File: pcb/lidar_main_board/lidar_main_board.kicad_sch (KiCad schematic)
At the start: 18 parts, among them J1 vl53l1x, J2 AS5600, J3 HC-06, J4 Bateria, U1 LPC845-BRK, U2 AMS1117-3.3, U3 LM7805_TO220

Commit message: add pcb
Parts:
- added A1: Pololu_Breakout_A4988, Module:Pololu_Breakout-16_15.2x20.3mm, symbol Driver_Motor:Pololu_Breakout_A4988
- added D2: LED, LED_THT:LED_D5.0mm, symbol Device:LED
- added J5: Boton 1, Connector_PinHeader_2.54mm:PinHeader_1x03_P2.54mm_Vertical, symbol Connector:Conn_01x03_Pin
- added J6: Boton 2, Connector_PinHeader_2.54mm:PinHeader_1x03_P2.54mm_Vertical, symbol Connector:Conn_01x03_Pin
- added J7: Boton 3, Connector_PinHeader_2.54mm:PinHeader_1x03_P2.54mm_Vertical, symbol Connector:Conn_01x03_Pin
- added J8: Motor, Connector_PinHeader_2.54mm:PinHeader_1x04_P2.54mm_Vertical, symbol Connector:Conn_01x04_Pin
- added R2: 33k, Resistor_THT:R_Axial_DIN0207_L6.3mm_D2.5mm_P10.16mm_Horizontal, symbol Device:R
- added R3: 20k, Resistor_THT:R_Axial_DIN0207_L6.3mm_D2.5mm_P10.16mm_Horizontal, symbol Device:R
- added R4: 120, Resistor_THT:R_Axial_DIN0207_L6.3mm_D2.5mm_P10.16mm_Horizontal, symbol Device:R
- D1: value LED -> LED_PWR
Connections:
- net +3V3: now also U1.40 (VDD), A1.13 (~{RESET}), A1.14 (~{SLEEP}), A1.2 (VDD), J5.1 (Pin_1), J6.1 (Pin_1), J7.1 (Pin_1), R4.1
- net +5V: now also J3.2 (Pin_2), A1.8 (VMOT); no longer J3.1 (Pin_1)
- net +BATT: now also J4.2 (Pin_2), R2.1; no longer J4.1 (Pin_1)
- net GND: now also J3.1 (Pin_1), J4.1 (Pin_1), U1.20 (GND), A1.1 (GND), A1.12 (MS3), A1.7 (GND), A1.9 (~{ENABLE}), J5.2 (Pin_2), J6.2 (Pin_2), J7.2 (Pin_2), R3.2; no longer J3.2 (Pin_2), J4.2 (Pin_2)
- net I2C1 - SCL: now also J2.3 (Pin_3), U1.7 (PIO0_22); no longer J2.4 (Pin_4)
- net I2C1 - SDA: now also J2.4 (Pin_4), U1.8 (PIO0_23); no longer J2.3 (Pin_3)
- net UART0 - RX: now also U1.2 (PIO0_17)
- net UART0 - TX: now also U1.1 (PIO0_16)
- net BTN_START: now reaches U1.15 (PIO0_29)
- net BTN_START: now also J5.3 (Pin_3)
- net BTN_SEL: now reaches U1.16 (PIO0_30)
- net BTN_SEL: now also J7.3 (Pin_3)
- net BTN_MODE: now reaches U1.17 (PIO0_31)
- net BTN_MODE: now also J6.3 (Pin_3)
- net DIR: now reaches U1.23 (PIO0_10)
- net DIR: now also A1.16 (DIR)
- net STEP: now reaches U1.24 (PIO0_11)
- net STEP: now also A1.15 (STEP)
- net MS2: now reaches U1.28 (PIO0_15)
- net MS2: now also A1.11 (MS2)
- net MS1: now reaches U1.29 (PIO1_2_RED_LED)
- net MS1: now also A1.10 (MS1)
- net BAT_ADC: now reaches U1.33 (PIO0_06)
- net BAT_ADC: now also R2.2, R3.1
- net LED_DIR: now reaches U1.36 (PIO0_03_SWCLK)
- net LED_DIR: now also D2.1 (K)
- new net: D2.2 (A), R4.2
- new net: A1.3 (1B), J8.1 (Pin_1)
- new net: A1.4 (1A), J8.2 (Pin_2)
- new net: A1.5 (2A), J8.3 (Pin_3)
- new net: A1.6 (2B), J8.4 (Pin_4)
- no-connect marks 0 -> 25
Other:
- note added: "Bateria"
- note added: "Leds"
- note added: "R1= R2 [( Vcc / Vadc) - 1] R2 = 20K Vcc = 2 * 4.2V = 8.4V Vadc = 3.2 V R1 = 32K5 = 33K"
- note added: "Vd = 1.2 V Id = (Vcc - Vd)/R1 Id = 17.5mA"
- moved on the sheet: C1, C2, C3, C4, C5, D1, H1, H2, H3, H4, J1, J2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

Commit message: new version pcb
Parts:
- removed J2: AS5600, Connector_PinHeader_2.54mm:PinHeader_1x04_P2.54mm_Vertical, symbol Connector:Conn_01x04_Pin
- added D3: LED, LED_THT:LED_D5.0mm, symbol Device:LED
- added J2: AS5600, Connector_PinHeader_2.54mm:PinHeader_1x05_P2.54mm_Vertical, symbol Connector:Conn_01x05_Pin
- added R5: 120, Resistor_THT:R_Axial_DIN0207_L6.3mm_D2.5mm_P10.16mm_Horizontal, symbol Device:R
- D1: value LED_PWR -> LED
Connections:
- net +3V3: no longer A1.13 (~{RESET}), A1.14 (~{SLEEP}), R4.1
- net +5V: now also J2.1 (Pin_1)
- net +BATT: now also J4.1 (Pin_1); no longer J4.2 (Pin_2)
- net BTN_MODE: now also U1.16 (PIO0_30); no longer U1.17 (PIO0_31)
- net BTN_SEL: now also U1.17 (PIO0_31); no longer U1.16 (PIO0_30)
- net DIR: now also R4.1, U1.22 (PIO0_09); no longer U1.23 (PIO0_10)
- net GND: now also D2.1 (K), J4.2 (Pin_2), D3.1 (K), J2.2 (Pin_2); no longer A1.12 (MS3), J4.1 (Pin_1)
- net I2C1 - SCL: now also U1.6 (PIO0_21), J2.3 (Pin_3); no longer U1.7 (PIO0_22)
- net I2C1 - SDA: now also U1.7 (PIO0_22), J2.4 (Pin_4); no longer U1.8 (PIO0_23)
- net STEP: now also U1.23 (PIO0_10), R5.1; no longer U1.24 (PIO0_11)
- net DIR_AS5600: now reaches U1.12 (PIO0_26)
- net DIR_AS5600: now also J2.5 (Pin_5)
- net MRESET: now reaches U1.26 (PIO0_13)
- net MRESET: now also A1.13 (~{RESET})
- net MS3: now reaches U1.27 (PIO0_14)
- net MS3: now also A1.12 (MS3)
- net LED_DIR: no longer names the net of U1.36 (PIO0_03_SWCLK)
- net LED_DIR: no longer D2.1 (K)
- new net: D3.2 (A), R5.2
- new net MSLEEP: A1.14 (~{SLEEP}), U1.24 (PIO0_11)
- no-connect marks 25 -> 22
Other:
- note added: "Vd = 1.2 V Vcc = 3.3 V Id = (Vcc - Vd)/R1 Id = 17.5mA"
- note removed: "Vd = 1.2 V Id = (Vcc - Vd)/R1 Id = 17.5mA"
- moved on the sheet: D1, D2, H1, H2, H3, H4, J1, J3, J4, J5, J6, J7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

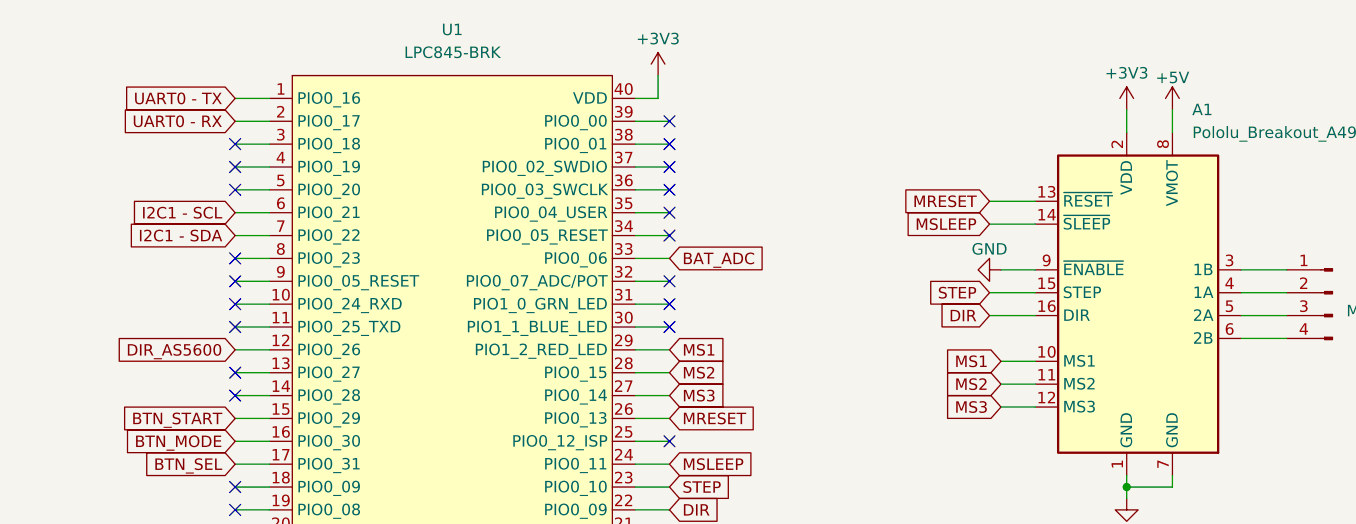
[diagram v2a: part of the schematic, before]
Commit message: molex in pcb
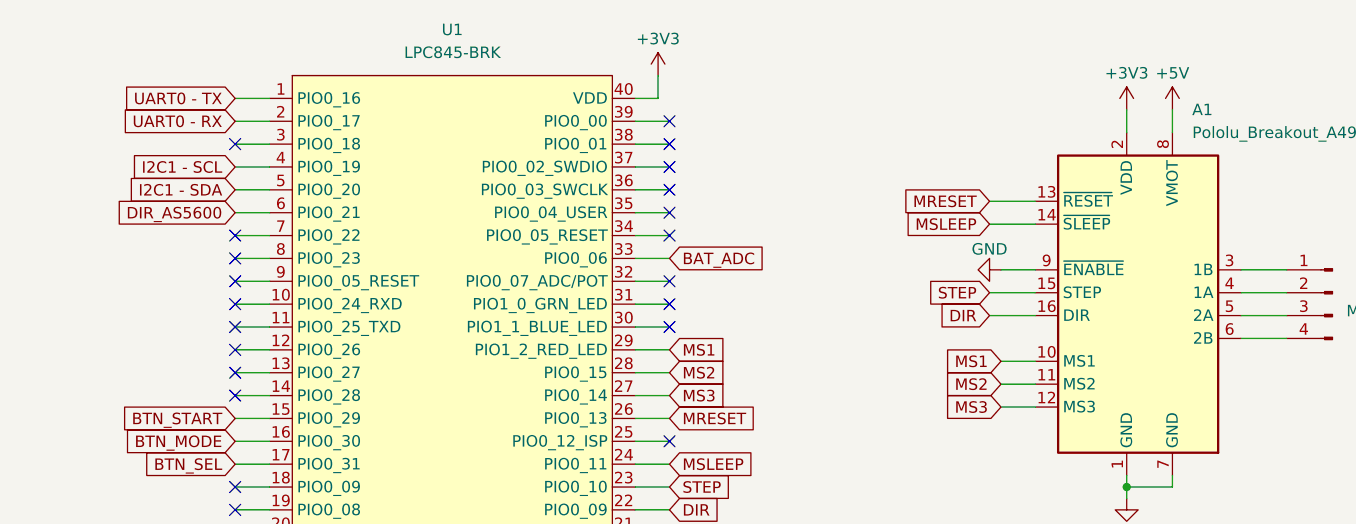
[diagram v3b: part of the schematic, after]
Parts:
- J1, J8: footprint Connector_PinHeader_2.54mm:PinHeader_1x04_P2.54mm_Vertical -> Connector_Molex:Molex_SL_171971-0004_1x04_P2.54mm_Vertical
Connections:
- net DIR_AS5600: now also U1.6 (PIO0_21); no longer U1.12 (PIO0_26)
- net I2C1 - SCL: now also U1.4 (PIO0_19); no longer U1.6 (PIO0_21)
- net I2C1 - SDA: now also U1.5 (PIO0_20); no longer U1.7 (PIO0_22)
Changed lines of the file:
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@@
 	)
 	(no_connect
-		(at 36.83 31.75)
+		(at 36.83 52.07)
 	)
 	(no_connect
-		(at 36.83 34.29)
+		(at 36.83 39.37)
 	)
 	(no_connect
@@
 	)
 	(no_connect
-		(at 36.83 29.21)
-	)
-	(no_connect
 		(at 85.09 31.75)
 	)
@@
 	)
 	(no_connect
+		(at 36.83 29.21)
+	)
+	(no_connect
 		(at 85.09 62.23)
 	)
@@
 		)
 	)
-	(global_label "MS1"
+	(global_label "DIR_AS5600"
 		(shape input)
-		(at 121.92 53.34 180)
+		(at 36.83 36.83 180)
 		(fields_autoplaced yes)
 		(effects
@@
 		)
 		(property "Intersheetrefs" "${INTERSHEET_REFS}"
-			(at 115.0644 53.34 0)
+			(at 22.5963 36.83 0)
 			(effects
 				(font
@@
 		)
 	)
-	(global_label "I2C1 - SCL"
+	(global_label "MS1"
 		(shape input)
-		(at 36.83 36.83 180)
+		(at 121.92 53.34 180)
 		(fields_autoplaced yes)
 		(effects
@@
 		)
 		(property "Intersheetrefs" "${INTERSHEET_REFS}"
-			(at 22.5358 36.83 0)
+			(at 115.0644 53.34 0)
 			(effects
 				(font
@@
 		)
 	)
-	(global_label "I2C1 - SCL"
+	(global_label "I2C1 - SDA"
 		(shape input)
-		(at 133.35 151.13 0)
+		(at 36.83 34.29 180)
 		(fields_autoplaced yes)
 		(effects
@@
 				(size 1.27 1.27)
 			)
-			(justify left)
+			(justify right)
 		)
 		(property "Intersheetrefs" "${INTERSHEET_REFS}"
-			(at 147.6442 151.13 0)
+			(at 22.4753 34.29 0)
 			(effects
 				(font
 					(size 1.27 1.27)
 				)
-				(justify left)
+				(justify right)
 				(hide yes)
 			)
 		)
 	)
-	(global_label "MSLEEP"
+	(global_label "I2C1 - SCL"
 		(shape input)
-		(at 120.65 38.1 180)
+		(at 133.35 151.13 0)
 		(fields_autoplaced yes)
 		(effects
@@
 				(size 1.27 1.27)
 			)
-			(justify right)
+			(justify left)
 		)
 		(property "Intersheetrefs" "${INTERSHEET_REFS}"
-			(at 110.4078 38.1 0)
+			(at 147.6442 151.13 0)
 			(effects
 				(font
 					(size 1.27 1.27)
 				)
-				(justify right)
+				(justify left)
 				(hide yes)
 			)
 		)
 	)
-	(global_label "DIR_AS5600"
+	(global_label "MSLEEP"
 		(shape input)
-		(at 36.83 52.07 180)
+		(at 120.65 38.1 180)
 		(fields_autoplaced yes)
 		(effects
@@
 		)
 		(property "Intersheetrefs" "${INTERSHEET_REFS}"
-			(at 22.5963 52.07 0)
+			(at 110.4078 38.1 0)
 			(effects
 				(font
@@
 		)
 	)
+	(global_label "I2C1 - SCL"
+		(shape input)
+		(at 36.83 31.75 180)
+		(fields_autoplaced yes)
+		(effects
+			(font
+				(size 1.27 1.27)
+			)
+			(justify right)
+		)
+		(property "Intersheetrefs" "${INTERSHEET_REFS}"
+			(at 22.5358 31.75 0)
+			(effects
+				(font
+					(size 1.27 1.27)
+				)
+				(justify right)
+				(hide yes)
+			)
+		)
+	)
 	(global_label "MRESET"
 		(shape input)
@@
 		)
 	)
-	(global_label "I2C1 - SDA"
-		(shape input)
-		(at 36.83 39.37 180)
-		(fields_autoplaced yes)
-		(effects
-			(font
-				(size 1.27 1.27)
-			)
-			(justify right)
-		)
-		(property "Intersheetrefs" "${INTERSHEET_REFS}"
-			(at 22.4753 39.37 0)
-			(effects
-				(font
-					(size 1.27 1.27)
-				)
-				(justify right)
-				(hide yes)
-			)
-		)
-	)
 	(global_label "MSLEEP"
 		(shape input)
@@
 			)
 		)
-		(property "Footprint" "Connector_PinHeader_2.54mm:PinHeader_1x04_P2.54mm_Vertical"
+		(property "Footprint" "Connector_Molex:Molex_SL_171971-0004_1x04_P2.54mm_Vertical"
 			(at 158.75 45.72 0)
 			(effects
@@
 			)
 		)
-		(property "Footprint" "Connector_PinHeader_2.54mm:PinHeader_1x04_P2.54mm_Vertical"
+		(property "Footprint" "Connector_Molex:Molex_SL_171971-0004_1x04_P2.54mm_Vertical"
 			(at 124.46 146.05 0)
 			(effects
@@
 		)
 		(property "Value" "+5V"
-			(at 140.97 21.844 0)
+			(at 140.97 21.336 0)
 			(effects
 				(font

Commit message: feat: pcb desing used
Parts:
- R2: value 33k -> 100k
- R3: value 20k -> 62k
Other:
- note added: "Modulos"
- note added: "R1= R2 [( Vcc / Vadc) - 1] R2 = 62K Vcc = 2 * 4.2V = 8.4V Vadc = 3.2 V R1 = 100.75k = 100k"
- note removed: "R1= R2 [( Vcc / Vadc) - 1] R2 = 20K Vcc = 2 * 4.2V = 8.4V Vadc = 3.2 V R1 = 32K5 = 33K"
- moved on the sheet: A1, D1, D2, D3, J8, R1, R4, R5, U1

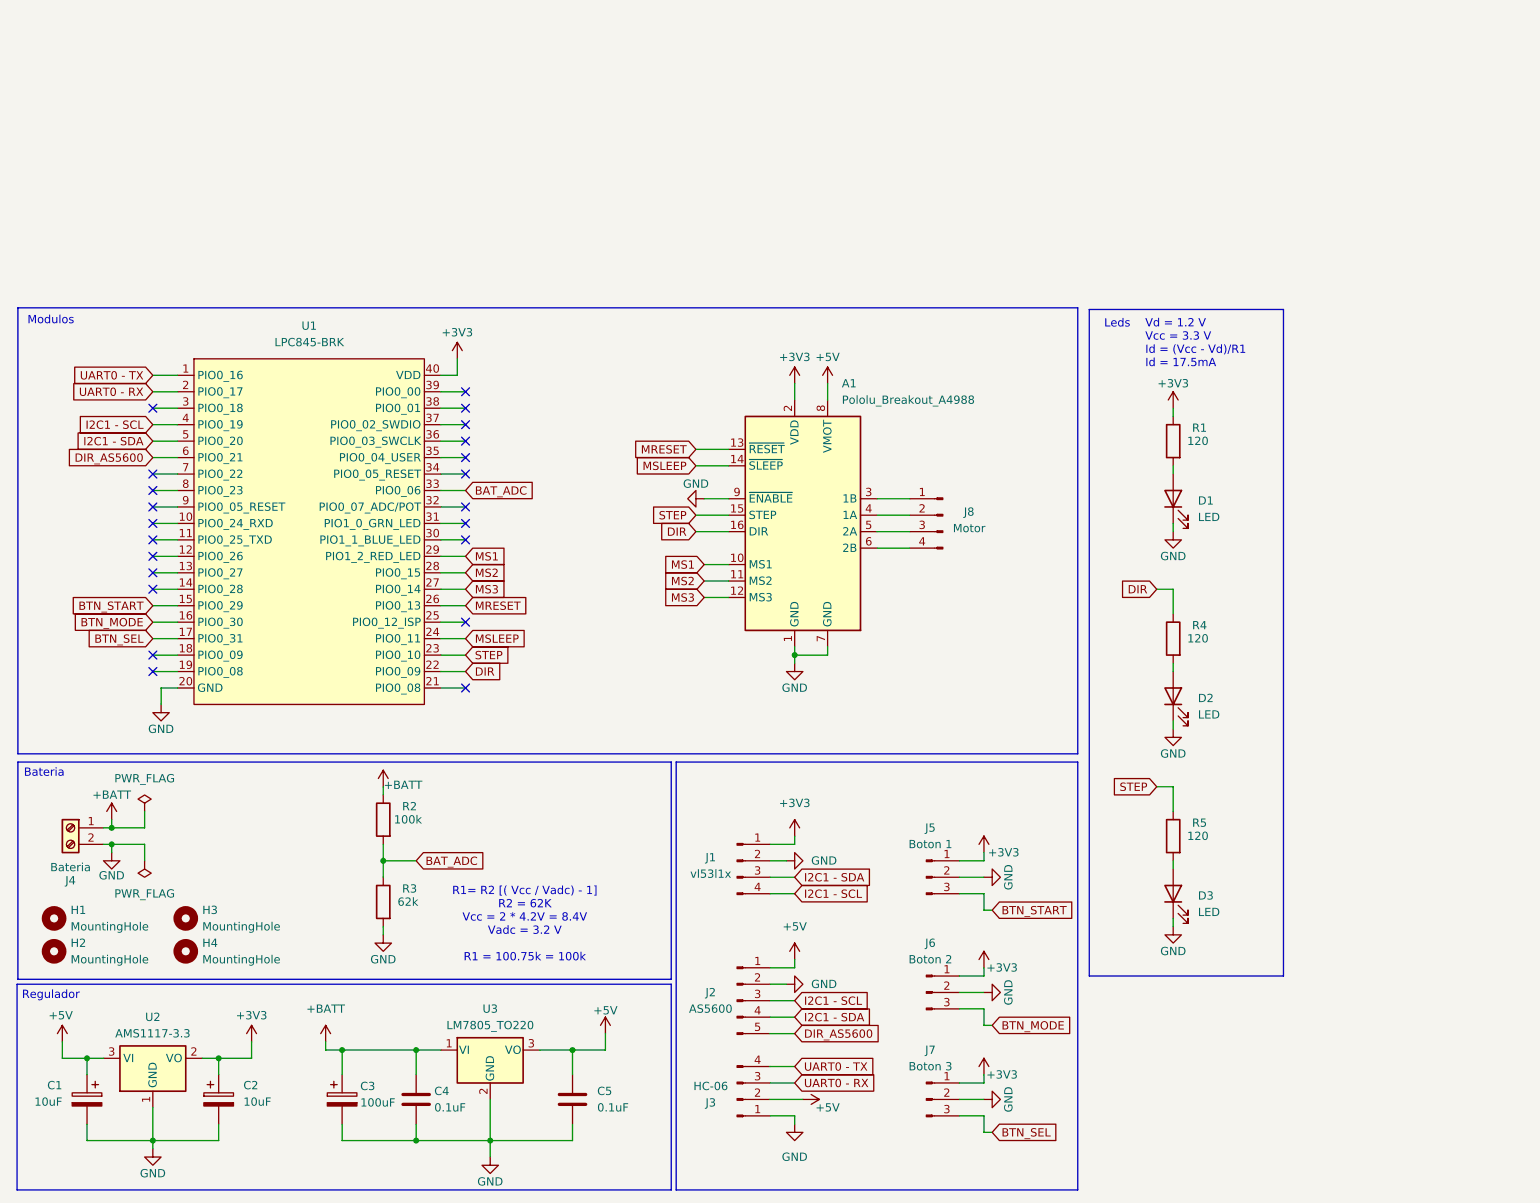
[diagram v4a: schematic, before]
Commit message: feat ADC to test and web page
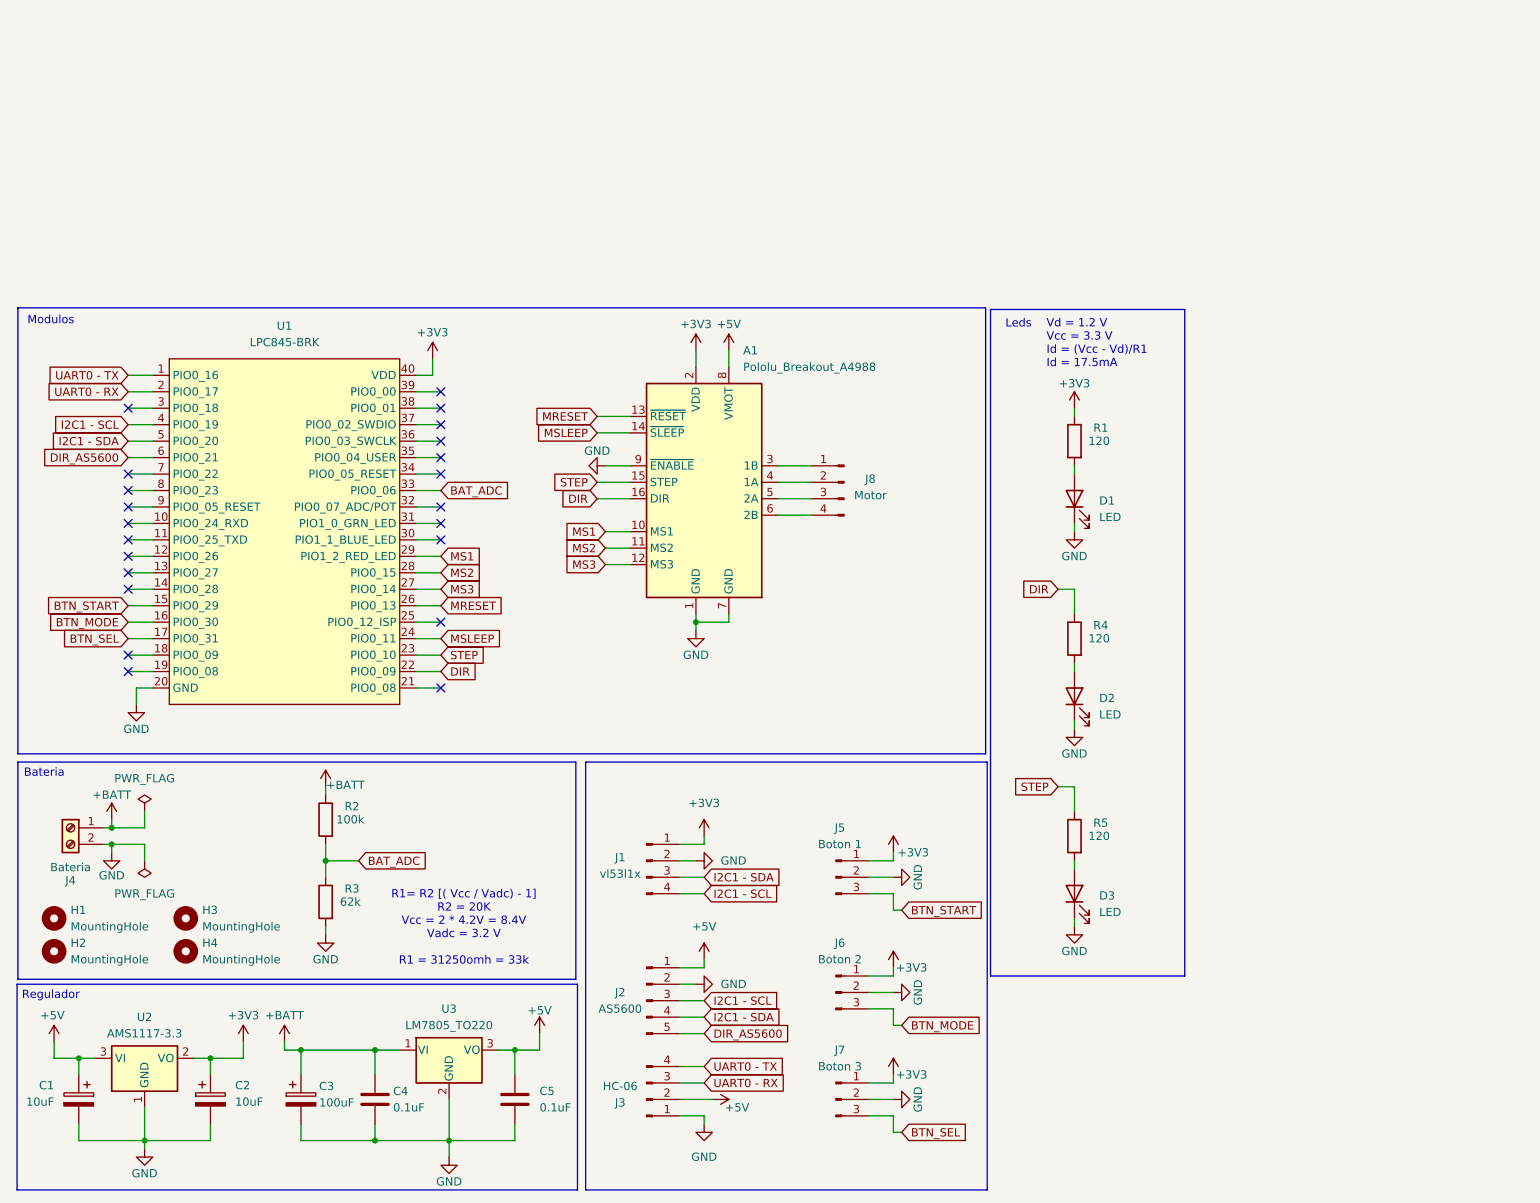
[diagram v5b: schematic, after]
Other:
- note added: "R1= R2 [( Vcc / Vadc) - 1] R2 = 20K Vcc = 2 * 4.2V = 8.4V Vadc = 3.2 V R1 = 31250omh = 33k"
- note removed: "R1= R2 [( Vcc / Vadc) - 1] R2 = 62K Vcc = 2 * 4.2V = 8.4V Vadc = 3.2 V R1 = 100.75k = 100k"
- moved on the sheet: A1, C1, C2, C3, C4, C5, D1, D2, D3, J1, J2, J3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
